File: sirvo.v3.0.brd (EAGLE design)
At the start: 17.5 x 33.9 mm, 35 parts

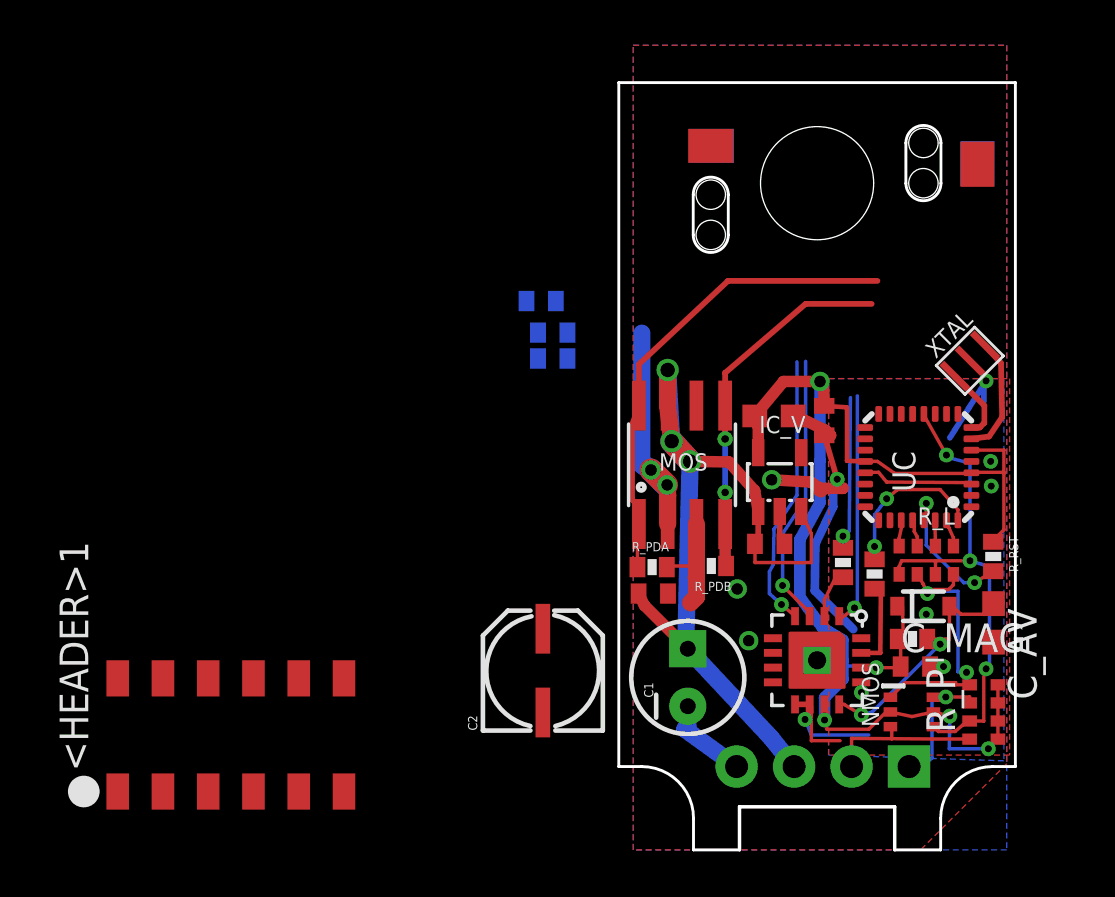
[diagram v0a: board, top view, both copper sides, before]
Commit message: Finished routing of all on-board signals
Header routing not yet completed
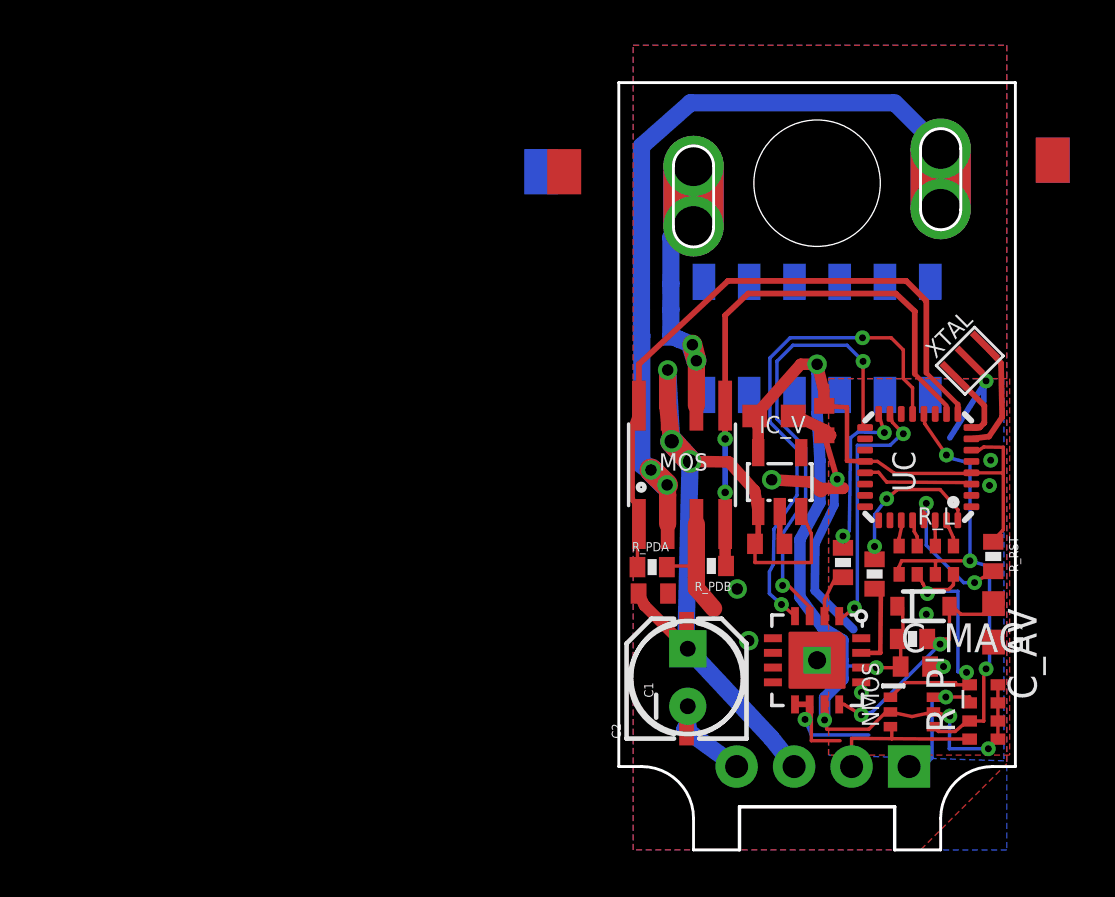
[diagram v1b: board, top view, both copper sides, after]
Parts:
- removed JP2, JP4: M01SMD-4.5X1.5, SparkFun-Connectors:PAD-1.5X4.5
- added JP5, JP6: M01SMD-4.5X1.5, SparkFun-Connectors:PAD-1.5X4.5
- moved <HEADER>1 31.3 mm to (37.3, 23.9), flipped to the bottom
- moved JP1 19.3 mm to (25.1, 31.2), flipped to the bottom
- moved JP3 18.3 mm to (26.2, 31.2), flipped to the top
- moved C2 6.36 mm to (31.4, 8.79)
- moved C_M1 5.14 mm to (30.2, 26.3), turned to 0 degrees
- moved C_M 4.68 mm to (30.2, 24.0)
- moved C_M2 4.68 mm to (30.2, 25.1)
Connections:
- net MOTOR_A: no longer JP1.P$1, JP3.P$1
- net MOTOR_B: no longer JP2.P$1, JP4.P$1
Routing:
- net MOTOR_B: track 9.92 -> 38.3 mm, vias 2 -> 4
- net AS5050_SS: track 12.1 -> 22.3 mm, vias 1 -> 2
- net MOTOR_A: track 0.00 -> 9.82 mm, vias 0 -> 2
- net MB_PWM: track 17.7 -> 26.8 mm
- net MA_PWM: track 21.2 -> 29.3 mm
- net SCK: track 12.1 -> 20.1 mm, vias 1 -> 2
- net N$4: track 0.00 -> 5.33 mm, vias 0 -> 2
- net 3.3V: track 60.2 -> 62.0 mm
- net MOSI: track 10.5 -> 11.7 mm, vias 1 -> 2
- net M_GND: track 14.2 -> 15.3 mm
- net MISO: track 6.77 -> 7.44 mm, vias 1 -> 2
- net VIN: track 38.8 -> 39.4 mm
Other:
- outline, holes or cut-outs redrawn
- board text added: "Optional LEDs over here?"

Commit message: Added header routing and silkscreen
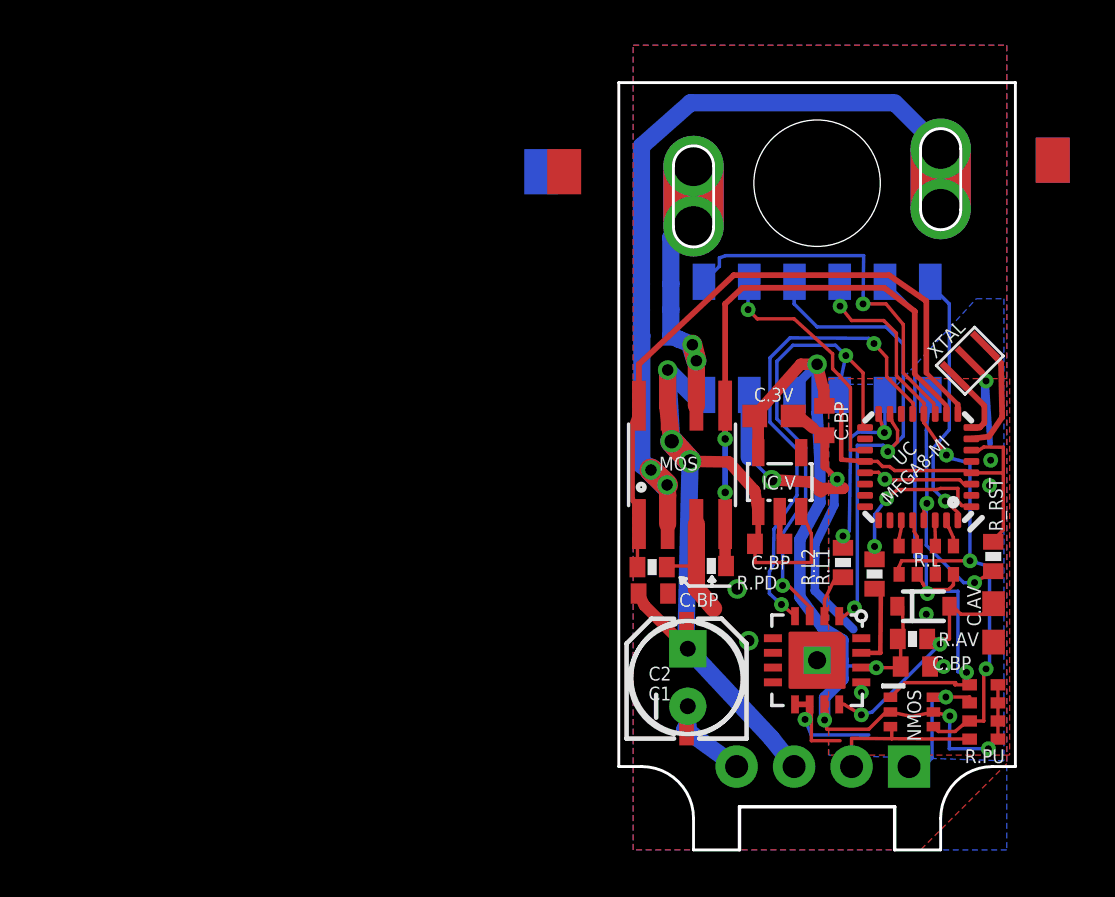
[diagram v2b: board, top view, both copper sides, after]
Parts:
- renumbered C_3V2 to C.3V, C_AV to C.AV, C_MAG to C.MAG, C_MOS to C.MOS, C_UC to C.UC, D_AV to D.AV, IC_V to IC.V, R_AV to R.AV, R_L to R.L, R_L1 to R.L1, R_L2 to R.L2, R_P to R.PU, R_PDA to R.PDA, R_PDB to R.PDB
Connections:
- removed net A6: UC.19
- removed net PD3: UC.1
- new net A6_HEADER_ADC: <HEADER>1.P$10, UC.19
- new net PD2_HEADER_HW_INT: <HEADER>1.P$2, UC.32
- net 3.3V: now also <HEADER>1.P$7
- net AS5050_INT: now also UC.1; no longer UC.32
- net MISO: now also <HEADER>1.P$3
- net MOSI: now also <HEADER>1.P$8
- net M_GND: now also <HEADER>1.P$9
- net PD7: now also <HEADER>1.P$12
- net RESET: now also <HEADER>1.P$1
- net SCK: now also <HEADER>1.P$5
- net SCL/TX0: now also <HEADER>1.P$4
- net SDA/RXI: now also <HEADER>1.P$6
- net VIN: now also <HEADER>1.P$11
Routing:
- net PD7: track 0.00 -> 16.6 mm, vias 0 -> 1
- net SCL/TX0: track 12.6 -> 27.5 mm
- net PD2_HEADER_HW_INT: track 0.00 -> 11.6 mm, vias 0 -> 1
- net MOSI: track 11.7 -> 23.3 mm
- net A6_HEADER_ADC: track 0.00 -> 11.0 mm, vias 0 -> 1
- net SDA/RXI: track 22.2 -> 30.4 mm, vias 3 -> 4
- net RESET: track 6.41 -> 11.4 mm
- net M_GND: track 15.3 -> 19.4 mm
- net VIN: track 39.4 -> 41.4 mm
- net 3.3V: track 62.0 -> 63.8 mm
- net MISO: track 7.44 -> 9.12 mm
- net SCK: track 20.1 -> 21.6 mm
- net AS5050_SS: track 22.3 -> 21.6 mm
- net GND: track 31.1 -> 30.5 mm, vias 8 -> 9
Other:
- board text added: "C.BP"
- board text added: "R.PD"
- board text removed: "C-REG"

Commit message: Routed Headers, added header pinout in silk
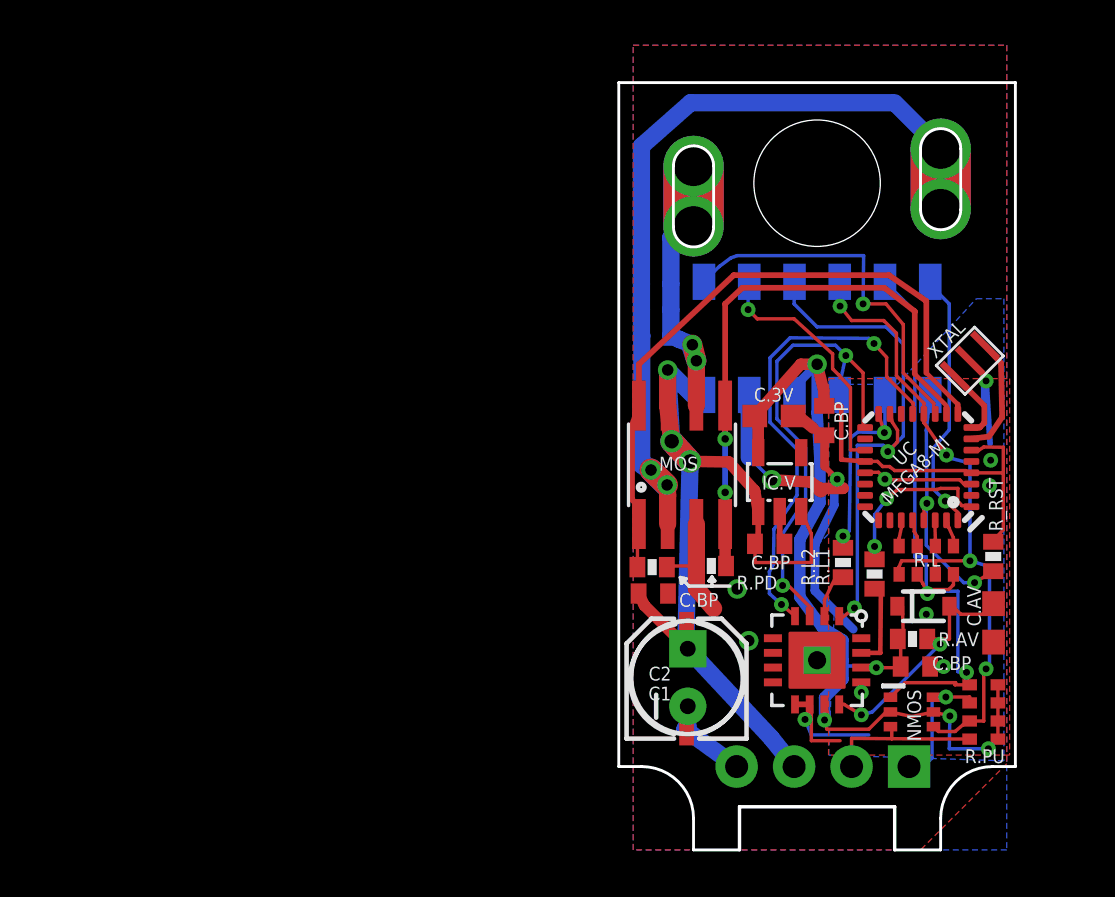
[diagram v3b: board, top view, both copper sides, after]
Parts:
- moved U$1 29.1 mm to (44.5, 7.75)
- moved JP1 6.68 mm to (31.8, 30.2)
- moved JP3 5.73 mm to (31.8, 30.0)
- moved JP5 4.89 mm to (42.9, 31.0)
- moved JP6 4.89 mm to (42.9, 31.0)
- renumbered <HEADER>1 to <HEADER>
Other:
- board text added: "C D"
- board text added: "D.0 TX RX MOSI A6 D.6"
- board text added: "RST MISO SCK 3.3V GND VIN"
- board text added: "SirVo v3.0 08APR2014 Tekdemo@gmail.com"
- board text removed: "SirVo V2.6 Tekdemo@gmail.com"

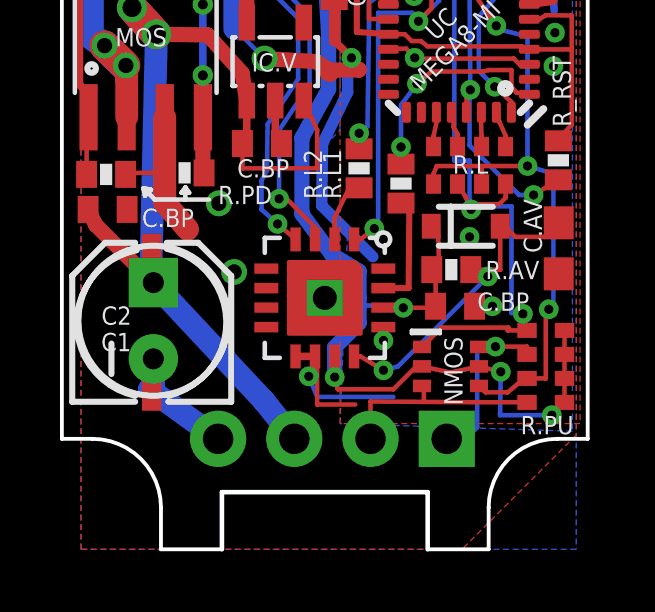
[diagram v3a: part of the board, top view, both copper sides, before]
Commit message: Board as-ordered for revision 3.0
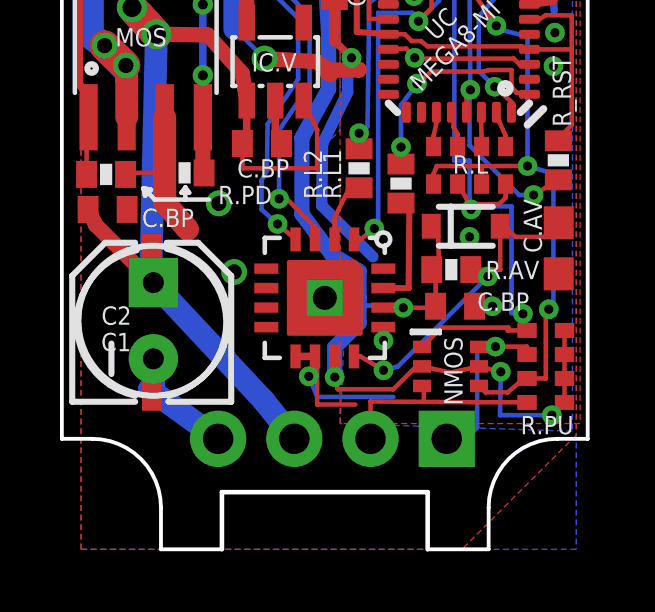
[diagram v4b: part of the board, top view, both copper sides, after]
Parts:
- moved U$1 1.42 mm to (45.8, 7.11)
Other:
- board text added: "D.2 TX RX MOSI A6 D.7"
- board text removed: "D.0 TX RX MOSI A6 D.6"
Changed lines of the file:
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@@
 <setting verticaltext="up"/>
 </settings>
-<grid distance="10" unitdist="mil" unit="mil" style="lines" multiple="5" display="yes" altdistance="1" altunitdist="mil" altunit="mil"/>
+<grid distance="0.05" unitdist="inch" unit="inch" style="lines" multiple="5" display="yes" altdistance="0.005" altunitdist="inch" altunit="inch"/>
 <layers>
-<layer number="1" name="Top" color="4" fill="10" visible="no" active="yes"/>
+<layer number="1" name="Top" color="4" fill="10" visible="yes" active="yes"/>
 <layer number="16" name="Bottom" color="1" fill="1" visible="yes" active="yes"/>
 <layer number="17" name="Pads" color="2" fill="1" visible="yes" active="yes"/>
@@
 <layer number="24" name="bOrigins" color="15" fill="1" visible="yes" active="yes"/>
 <layer number="25" name="tNames" color="13" fill="1" visible="no" active="yes"/>
-<layer number="26" name="bNames" color="7" fill="1" visible="yes" active="yes"/>
+<layer number="26" name="bNames" color="7" fill="1" visible="no" active="yes"/>
 <layer number="27" name="tValues" color="10" fill="1" visible="no" active="yes"/>
 <layer number="28" name="bValues" color="7" fill="1" visible="no" active="yes"/>
@@
 <layer number="49" name="Reference" color="7" fill="1" visible="no" active="yes"/>
 <layer number="50" name="dxf" color="7" fill="1" visible="no" active="yes"/>
-<layer number="51" name="tDocu" color="6" fill="13" visible="no" active="yes"/>
-<layer number="52" name="bDocu" color="7" fill="1" visible="yes" active="yes"/>
+<layer number="51" name="tDocu" color="6" fill="13" visible="yes" active="yes"/>
+<layer number="52" name="bDocu" color="7" fill="1" visible="no" active="yes"/>
 <layer number="53" name="tGND_GNDA" color="7" fill="9" visible="no" active="no"/>
 <layer number="54" name="bGND_GNDA" color="1" fill="9" visible="no" active="no"/>
@@
 <text x="38.7096" y="19.3548" size="0.6096" layer="25" font="vector" ratio="16" rot="R90">C.BP</text>
 <text x="42.418" y="9.2202" size="0.6096" layer="25" font="vector" ratio="16">C.BP</text>
-<circle x="42.291" y="19.685" radius="0.523634375" width="0" layer="22"/>
 <text x="43.0022" y="22.3774" size="0.6096" layer="22" font="vector" ratio="15" distance="225" rot="MR90" align="top-left">RST
 MISO
@@
 GND
 VIN</text>
-<text x="42.2148" y="25.5016" size="0.6096" layer="22" font="vector" ratio="15" distance="228" rot="MR90" align="top-right">D.0
+<text x="42.2148" y="25.5016" size="0.6096" layer="22" font="vector" ratio="15" distance="228" rot="MR90" align="top-right">D.2
 TX
 RX
 MOSI
 A6
-D.6</text>
+D.7</text>
 <text x="42.9768" y="25.5016" size="0.6096" layer="22" font="vector" ratio="15" distance="228" rot="MR90" align="top-right">
 C
@@
 <attribute name="VALUE" x="38.1" y="13.2715" size="0.6096" layer="27" ratio="16" rot="R270"/>
 </element>
-<element name="U$1" library="tekdemo" package="LOGO-SIRVO-GOLD" value="" x="44.5262" y="7.747" rot="MR0"/>
+<element name="U$1" library="tekdemo" package="LOGO-SIRVO-GOLD" value="" x="45.7962" y="7.112" rot="MR0"/>
 <element name="&lt;HEADER&gt;" library="tekdemo" package="M2X06_SMD" value="M06X022MM_SMT" x="37.338" y="23.876" smashed="yes" rot="MR0">
-<attribute name="NAME" x="43.511" y="20.7012" size="0.889" layer="26" rot="MR90"/>
+<attribute name="NAME" x="43.892" y="20.7012" size="0.889" layer="26" rot="MR90"/>
 </element>
 <element name="C1" library="SparkFun-Passives" package="CPOL-RADIAL-10UF-25V" value="" x="31.623" y="8.89" smashed="yes" rot="R90">
@@
 <vertex x="45.593" y="5.207"/>
 <vertex x="37.846" y="5.461"/>
-<vertex x="38.1" y="11.938"/>
+<vertex x="38.1" y="10.668"/>
 <vertex x="37.338" y="12.7"/>
 <vertex x="37.338" y="14.732"/>

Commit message: verified functionality of board, added notes
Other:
- board text added: "MOVE MOTOR CAPS, THEY INTERFERE WITH SERVO LID"
- board text removed: "15"
- board text removed: "Size of a quarter (for scale)"
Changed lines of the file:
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@@
 <setting verticaltext="up"/>
 </settings>
-<grid distance="0.05" unitdist="inch" unit="inch" style="lines" multiple="5" display="yes" altdistance="0.005" altunitdist="inch" altunit="inch"/>
+<grid distance="10" unitdist="mil" unit="mil" style="lines" multiple="5" display="yes" altdistance="1" altunitdist="mil" altunit="mil"/>
 <layers>
 <layer number="1" name="Top" color="4" fill="10" visible="yes" active="yes"/>
@@
 <layer number="27" name="tValues" color="10" fill="1" visible="no" active="yes"/>
 <layer number="28" name="bValues" color="7" fill="1" visible="no" active="yes"/>
-<layer number="29" name="tStop" color="7" fill="3" visible="no" active="yes"/>
-<layer number="30" name="bStop" color="7" fill="6" visible="no" active="yes"/>
+<layer number="29" name="tStop" color="7" fill="3" visible="yes" active="yes"/>
+<layer number="30" name="bStop" color="7" fill="6" visible="yes" active="yes"/>
 <layer number="31" name="tCream" color="7" fill="4" visible="no" active="yes"/>
 <layer number="32" name="bCream" color="7" fill="5" visible="no" active="yes"/>
@@
 <wire x1="37.338" y1="10.16" x2="37.338" y2="9.144" width="0.1524" layer="51"/>
 <wire x1="36.83" y1="9.652" x2="37.846" y2="9.652" width="0.1524" layer="51"/>
-<text x="51.562" y="11.684" size="0.6096" layer="51" font="vector" ratio="16">DIODE</text>
+<text x="48.514" y="11.43" size="0.6096" layer="51" font="vector" ratio="16">DIODE</text>
 <text x="28.956" y="5.588" size="0.6096" layer="22" font="vector" ratio="15" rot="MR90">SirVo v3.0 08APR2014
 Tekdemo@gmail.com</text>
-<text x="52.324" y="9.525" size="0.6096" layer="27" font="vector" ratio="16">15</text>
 <wire x1="33.909" y1="3.175" x2="40.767" y2="3.175" width="0.1524" layer="20"/>
 <wire x1="40.767" y1="3.175" x2="40.767" y2="1.27" width="0.1524" layer="20"/>
 <wire x1="33.909" y1="3.175" x2="33.909" y2="1.27" width="0.1524" layer="20"/>
-<circle x="59.182" y="13.208" radius="12.065" width="0.254" layer="51"/>
-<text x="54.61" y="25.4" size="0.6096" layer="51" font="vector" ratio="16">Size of a quarter
-(for scale)</text>
 <wire x1="30.988" y1="28.8036" x2="30.988" y2="31.496" width="0.127" layer="20"/>
 <wire x1="30.988" y1="31.496" x2="32.766" y2="31.496" width="0.127" layer="20" curve="-180"/>
@@
 <wire x1="42.799" y1="32.258" x2="42.799" y2="29.591" width="2.667" layer="29"/>
 <wire x1="42.799" y1="32.258" x2="42.799" y2="29.591" width="2.667" layer="30"/>
-<dimension x1="46.101" y1="32.9946" x2="43.561" y2="33.7566" x3="44.831" y3="39.116" textsize="1.778" textratio="15" layer="51" dtype="horizontal" unit="mil"/>
-<dimension x1="31.115" y1="33.1216" x2="28.575" y2="33.1216" x3="29.845" y3="39.243" textsize="1.778" textratio="15" layer="51" unit="mil"/>
+<dimension x1="46.101" y1="32.9946" x2="43.561" y2="33.7566" x3="44.831" y3="39.116" textsize="1.778" textratio="15" layer="47" dtype="horizontal" unit="mil"/>
+<dimension x1="31.115" y1="33.1216" x2="28.575" y2="33.1216" x3="29.845" y3="39.243" textsize="1.778" textratio="15" layer="47" unit="mil"/>
 <text x="48.514" y="21.59" size="0.6096" layer="51" font="vector" ratio="16" rot="R90">Optional LEDs
  over here?</text>
@@
 D
 </text>
+<text x="8.636" y="37.592" size="1.778" layer="51" font="vector" ratio="15">MOVE MOTOR CAPS,
+THEY INTERFERE WITH SERVO LID</text>
 </plain>
 <attributes>
@@
 </element>
 <element name="C.UC" library="rcl" package="C0402" value="0.1uF" x="37.6555" y="20.2438" smashed="yes" rot="R270">
-<attribute name="NAME" x="25.50795" y="21.67255" size="0.6096" layer="51" font="vector" ratio="16" rot="R90"/>
+<attribute name="NAME" x="25.76195" y="20.40255" size="0.6096" layer="51" font="vector" ratio="16" rot="R90"/>
 <attribute name="VALUE" x="39.3446" y="19.1516" size="0.6096" layer="27" ratio="16" rot="R90"/>
 </element>
@@
 </element>
 <element name="MOS" library="tekdemo" package="SO08" value="MOSFET-ARRAYMOSFET-ARRAY-H-BRIDGE" x="31.369" y="18.288" smashed="yes">
-<attribute name="VALUE" x="17.399" y="12.065" size="0.6096" layer="51" ratio="16" rot="R90"/>
+<attribute name="VALUE" x="27.051" y="16.383" size="0.6096" layer="51" ratio="16" rot="R90"/>
 <attribute name="NAME" x="30.353" y="18.034" size="0.6096" layer="25" ratio="16"/>
 </element>
